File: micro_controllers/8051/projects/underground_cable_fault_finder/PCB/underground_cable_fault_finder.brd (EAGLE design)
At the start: 160 x 100 mm, 73 parts, among them IC1 AT89S51, IC2 7805TV, IC3 adc804, T1 BC547, T2 BC547, T3 BC547

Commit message: 
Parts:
- removed CONN-6, CONN-7: 3 pin, con-amp-quick:03P
- removed CONNECTOR-5: 4 pin, con-amp-quick:04P
- removed D1, D2, D3: 1N4007, diode:DO41-10
- removed LED3, LED4, LED5: 5MM, led:LED5MM
- removed R16, R17, R21: 1K, rcl:0204/7
- removed R18, R19, R20: 5.6K, rcl:0204/7
- removed RELAY-1, RELAY-2, RELAY-3: 12V, relay:G5LE
- removed SL3: LM35, con-amp-quick:03P
- removed T1, T2, T3: BC547, transistor:TO92
- added SL1: (no value), con-amp-quick:03P
- SL2: device con-amp-quick:02P -> con-amp-quick:08P
- moved S10 201.3 mm to (102.9, 110.5), turned to 270 degrees
- moved CONNECTOR 191.1 mm to (120.7, 40.6), turned to 270 degrees
- moved S14 166.4 mm to (102.9, 129.5), turned to 270 degrees
- moved VR 155.7 mm to (55.9, 74.9)
- moved R7 153.3 mm to (83.8, 88.9)
- moved R15 142.3 mm to (82.5, 128.3)
- moved R10 141.0 mm to (41.9, 109.2)
- moved S5 135.3 mm to (102.9, 88.9), turned to 270 degrees
- moved S7 125.8 mm to (63.5, 110.5), turned to 270 degrees
- moved AVRCONNECTOR 124.3 mm to (22.9, 36.8), turned to 270 degrees
- moved S3 123.0 mm to (24.1, 88.9), turned to 90 degrees
- moved C1 118.8 mm to (0.00, 11.4)
- moved C6 117.7 mm to (6.35, 36.8), turned to 270 degrees
- moved S13 117.2 mm to (63.5, 129.5), turned to 270 degrees
- moved C2 109.9 mm to (0.00, 29.2), turned to 90 degrees
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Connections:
- removed net N$15: C5.1, C6.2, CONN-7.1, CONN-7.2, CONN-7.3, CONNECTOR-5.4, CONNECTOR.15, CONNECTOR.2, IC1.31, IC1.40, IC2.3, IC3.20, RN10.1, S2.2, SL2.1, SL3.1, SL8.2, SL8.3, SL8.4, SL8.5, VR.1, VR1.1
- removed net N$24: IC1.37, RN10.4
- removed net N$4: C3.2, C4.1, CONN-6.1, CONN-6.2, CONN-6.3, CONNECTOR-5.3, D1.C, D2.C, D3.C, IC2.1, R16.2, R17.2, R2.2, R21.1, RELAY-1.1, RELAY-2.1, RELAY-3.1, S1.5
- removed net N$41: R8.2, S9.2
- removed net N$65: D1.A, LED3.K, RELAY-1.2, T2.3
- removed net N$67: R19.1, T1.2
- removed net N$68: R18.1, T2.2
- removed net N$69: LED3.A, R17.1
- removed net N$70: LED4.A, R16.1
- removed net N$72: R8.1, RELAY-1.P
- removed net N$73: R12.1, RELAY-2.P
- removed net N$75: D2.A, LED4.K, RELAY-2.2, T1.3
- removed net N$77: D3.A, LED5.K, RELAY-3.2, T3.3
- removed net N$78: R20.1, T3.2
- removed net N$79: LED5.A, R21.2
- removed net N$80: R4.1, RELAY-3.P
- new net N$26: IC1.15, IC3.3
- new net N$39: IC3.6, SL2.1
- new net N$71: C3.2, C4.1, IC2.1, R2.2, S1.5, SL2.7, SL2.8
- new net N$76: R12.2, S11.2, SL2.4
- net N$19: now also R4.2, S8.2, SL2.2; no longer IC3.6, SL3.2
- net N$20: now also C6.2, CONNECTOR.15, CONNECTOR.2, IC1.31, IC1.40, RN10.1, S2.2, VR.1
- net N$21: now also R8.2, S9.2, SL2.3; no longer R4.2, S8.2
- net N$25: now also SL1.2; no longer R18.2
- net N$3: now also R12.1, R4.1, R8.1, SL2.5, SL2.6; no longer CONNECTOR-5.1, CONNECTOR-5.2, RELAY-1.S, RELAY-2.S, RELAY-3.S, SL2.2, SL3.3, T1.1, T2.1, T3.1
- net N$49: now also R10.2
- net N$53: now also R11.2
- net N$57: now also C5.1, IC2.3, IC3.20, S2.3, VR1.1; no longer R12.2, S11.2
- net N$61: now also R15.2
- net N$74: now also IC1.37, RN10.4, SL1.1; no longer R20.2
- net N$83: now also SL1.3; no longer R19.2
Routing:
- net N$3: track 0.00 -> 1070.6 mm
- net N$20: track 0.00 -> 727.7 mm, vias 0 -> 2
- net N$71: track 0.00 -> 264.2 mm
- net N$14: track 0.00 -> 133.9 mm
- net N$57: track 0.00 -> 116.1 mm
- net N$30: track 0.00 -> 113.3 mm
- net N$31: track 0.00 -> 106.5 mm
- net N$32: track 0.00 -> 99.6 mm
- net N$51: track 0.00 -> 93.8 mm
- net N$35: track 0.00 -> 86.5 mm
- net N$52: track 0.00 -> 86.1 mm, vias 0 -> 2
- net N$26: track 0.00 -> 79.9 mm
- net N$54: track 0.00 -> 79.6 mm
- net N$39: track 0.00 -> 78.5 mm, vias 0 -> 4
- net N$48: track 0.00 -> 74.8 mm
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- added copper zone on layer 16, net N$4
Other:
- board size 160 x 100 mm -> 182.9 x 135.6 mm

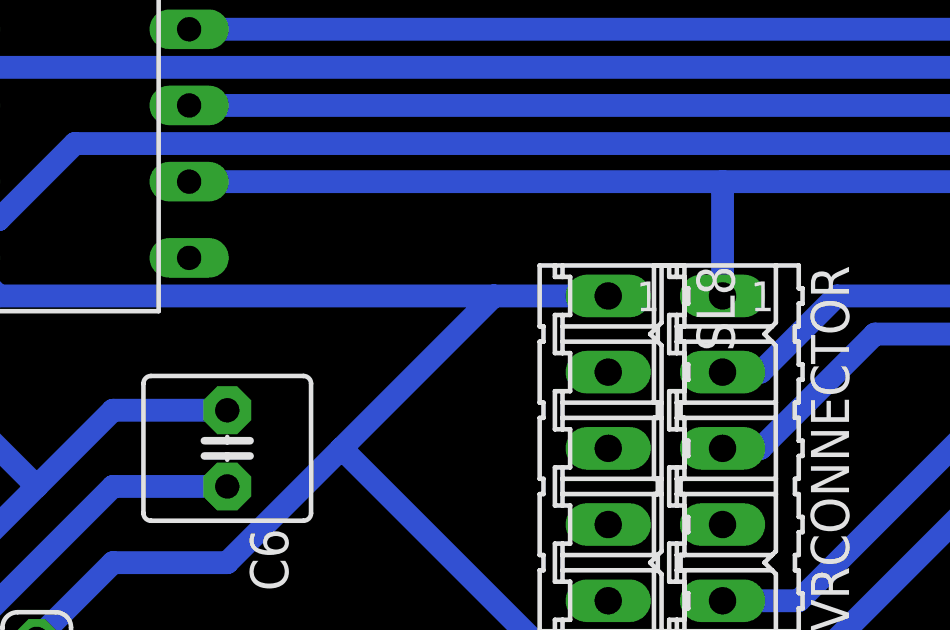
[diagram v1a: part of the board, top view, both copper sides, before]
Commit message: 
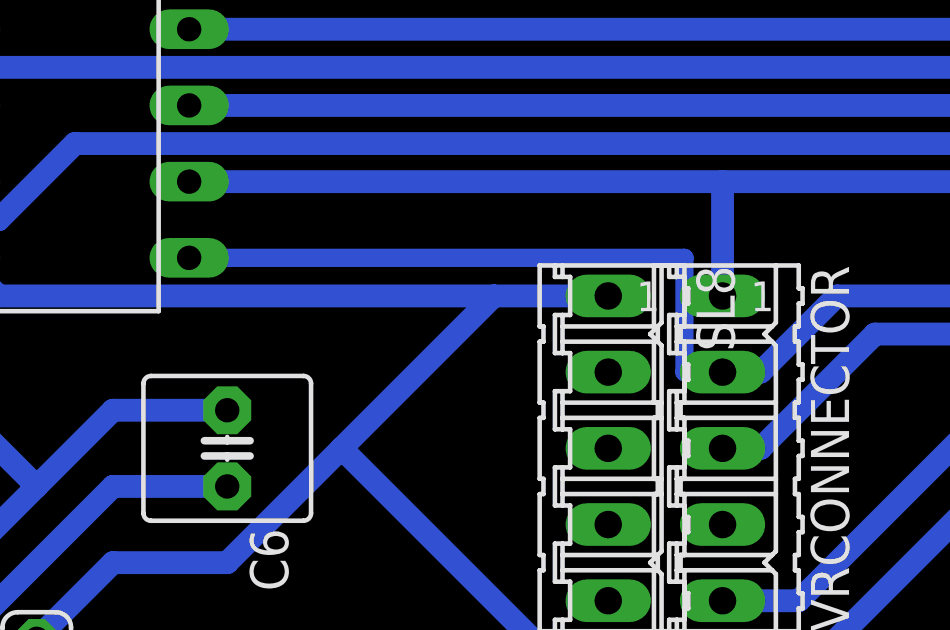
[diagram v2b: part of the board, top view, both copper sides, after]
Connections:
- removed net N$13: IC3.11
- net N$45: now also IC3.11
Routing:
- net N$45: track 13.0 -> 35.9 mm
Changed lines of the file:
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@@
 <?xml version="1.0" encoding="utf-8"?>
 <!DOCTYPE eagle SYSTEM "eagle.dtd">
-<eagle version="6.5.0">
+<eagle version="7.1.0">
 <drawing>
 <settings>
@@
 <grid distance="0.05" unitdist="inch" unit="inch" style="lines" multiple="1" display="no" altdistance="0.025" altunitdist="inch" altunit="inch"/>
 <layers>
-<layer number="1" name="Top" color="4" fill="1" visible="no" active="yes"/>
+<layer number="1" name="Top" color="4" fill="1" visible="yes" active="yes"/>
 <layer number="2" name="Route2" color="1" fill="3" visible="no" active="no"/>
 <layer number="3" name="Route3" color="4" fill="3" visible="no" active="no"/>
@@
 <layer number="19" name="Unrouted" color="6" fill="1" visible="yes" active="yes"/>
 <layer number="20" name="Dimension" color="15" fill="1" visible="yes" active="yes"/>
-<layer number="21" name="tPlace" color="7" fill="1" visible="no" active="yes"/>
-<layer number="22" name="bPlace" color="7" fill="1" visible="no" active="yes"/>
-<layer number="23" name="tOrigins" color="15" fill="1" visible="no" active="yes"/>
-<layer number="24" name="bOrigins" color="15" fill="1" visible="no" active="yes"/>
-<layer number="25" name="tNames" color="7" fill="1" visible="no" active="yes"/>
-<layer number="26" name="bNames" color="7" fill="1" visible="no" active="yes"/>
-<layer number="27" name="tValues" color="7" fill="1" visible="no" active="yes"/>
-<layer number="28" name="bValues" color="7" fill="1" visible="no" active="yes"/>
-<layer number="29" name="tStop" color="7" fill="3" visible="no" active="yes"/>
-<layer number="30" name="bStop" color="7" fill="6" visible="no" active="yes"/>
-<layer number="31" name="tCream" color="7" fill="4" visible="no" active="yes"/>
-<layer number="32" name="bCream" color="7" fill="5" visible="no" active="yes"/>
-<layer number="33" name="tFinish" color="6" fill="3" visible="no" active="yes"/>
-<layer number="34" name="bFinish" color="6" fill="6" visible="no" active="yes"/>
-<layer number="35" name="tGlue" color="7" fill="4" visible="no" active="yes"/>
-<layer number="36" name="bGlue" color="7" fill="5" visible="no" active="yes"/>
-<layer number="37" name="tTest" color="7" fill="1" visible="no" active="yes"/>
-<layer number="38" name="bTest" color="7" fill="1" visible="no" active="yes"/>
-<layer number="39" name="tKeepout" color="4" fill="11" visible="no" active="yes"/>
-<layer number="40" name="bKeepout" color="1" fill="11" visible="no" active="yes"/>
-<layer number="41" name="tRestrict" color="4" fill="10" visible="no" active="yes"/>
-<layer number="42" name="bRestrict" color="1" fill="10" visible="no" active="yes"/>
-<layer number="43" name="vRestrict" color="2" fill="10" visible="no" active="yes"/>
-<layer number="44" name="Drills" color="7" fill="1" visible="no" active="yes"/>
-<layer number="45" name="Holes" color="7" fill="1" visible="no" active="yes"/>
-<layer number="46" name="Milling" color="3" fill="1" visible="no" active="yes"/>
-<layer number="47" name="Measures" color="7" fill="1" visible="no" active="yes"/>
-<layer number="48" name="Document" color="7" fill="1" visible="no" active="yes"/>
-<layer number="49" name="Reference" color="7" fill="1" visible="no" active="yes"/>
-<layer number="51" name="tDocu" color="7" fill="1" visible="no" active="yes"/>
-<layer number="52" name="bDocu" color="7" fill="1" visible="no" active="yes"/>
+<layer number="21" name="tPlace" color="7" fill="1" visible="yes" active="yes"/>
+<layer number="22" name="bPlace" color="7" fill="1" visible="yes" active="yes"/>
+<layer number="23" name="tOrigins" color="15" fill="1" visible="yes" active="yes"/>
+<layer number="24" name="bOrigins" color="15" fill="1" visible="yes" active="yes"/>
+<layer number="25" name="tNames" color="7" fill="1" visible="yes" active="yes"/>
+<layer number="26" name="bNames" color="7" fill="1" visible="yes" active="yes"/>
+<layer number="27" name="tValues" color="7" fill="1" visible="yes" active="yes"/>
+<layer number="28" name="bValues" color="7" fill="1" visible="yes" active="yes"/>
+<layer number="29" name="tStop" color="7" fill="3" visible="yes" active="yes"/>
+<layer number="30" name="bStop" color="7" fill="6" visible="yes" active="yes"/>
+<layer number="31" name="tCream" color="7" fill="4" visible="yes" active="yes"/>
+<layer number="32" name="bCream" color="7" fill="5" visible="yes" active="yes"/>
+<layer number="33" name="tFinish" color="6" fill="3" visible="yes" active="yes"/>
+<layer number="34" name="bFinish" color="6" fill="6" visible="yes" active="yes"/>
+<layer number="35" name="tGlue" color="7" fill="4" visible="yes" active="yes"/>
+<layer number="36" name="bGlue" color="7" fill="5" visible="yes" active="yes"/>
+<layer number="37" name="tTest" color="7" fill="1" visible="yes" active="yes"/>
+<layer number="38" name="bTest" color="7" fill="1" visible="yes" active="yes"/>
+<layer number="39" name="tKeepout" color="4" fill="11" visible="yes" active="yes"/>
+<layer number="40" name="bKeepout" color="1" fill="11" visible="yes" active="yes"/>
+<layer number="41" name="tRestrict" color="4" fill="10" visible="yes" active="yes"/>
+<layer number="42" name="bRestrict" color="1" fill="10" visible="yes" active="yes"/>
+<layer number="43" name="vRestrict" color="2" fill="10" visible="yes" active="yes"/>
+<layer number="44" name="Drills" color="7" fill="1" visible="yes" active="yes"/>
+<layer number="45" name="Holes" color="7" fill="1" visible="yes" active="yes"/>
+<layer number="46" name="Milling" color="3" fill="1" visible="yes" active="yes"/>
+<layer number="47" name="Measures" color="7" fill="1" visible="yes" active="yes"/>
+<layer number="48" name="Document" color="7" fill="1" visible="yes" active="yes"/>
+<layer number="49" name="Reference" color="7" fill="1" visible="yes" active="yes"/>
+<layer number="51" name="tDocu" color="7" fill="1" visible="yes" active="yes"/>
+<layer number="52" name="bDocu" color="7" fill="1" visible="yes" active="yes"/>
 <layer number="91" name="Nets" color="2" fill="1" visible="no" active="no"/>
 <layer number="92" name="Busses" color="1" fill="1" visible="no" active="no"/>
@@
 <pass name="Default">
 <param name="RoutingGrid" value="50mil"/>
+<param name="AutoGrid" value="1"/>
+<param name="Efforts" value="0"/>
+<param name="TopRouterVariant" value="1"/>
 <param name="tpViaShape" value="round"/>
 <param name="PrefDir.1" value="0"/>
@@
 <wire x1="24.13" y1="39.37" x2="26.67" y2="41.91" width="0.762" layer="16"/>
 <wire x1="22.86" y1="39.37" x2="24.13" y2="39.37" width="0.762" layer="16"/>
+<contactref element="IC3" pad="11"/>
+<wire x1="5.08" y1="43.18" x2="21.59" y2="43.18" width="0.6096" layer="16"/>
+<wire x1="21.59" y1="43.18" x2="21.59" y2="39.37" width="0.6096" layer="16"/>
+<wire x1="21.59" y1="39.37" x2="24.13" y2="39.37" width="0.6096" layer="16"/>
 </signal>
 <signal name="N$5">
@@
 <wire x1="22.86" y1="45.72" x2="22.86" y2="41.91" width="0.762" layer="16"/>
 </signal>
-<signal name="N$13">
-<contactref element="IC3" pad="11"/>
-</signal>
 <signal name="N$17">
